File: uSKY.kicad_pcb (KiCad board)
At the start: 2 copper layers, 11.2 x 8.4 mm, 36 parts, among them U1 CC2510, X1 SMD_CRYSTAL_4PIN

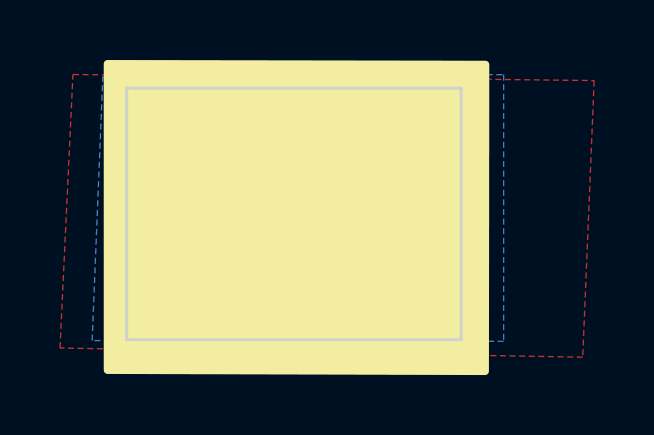
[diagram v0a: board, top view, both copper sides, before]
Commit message: removed silkscreen filled zone
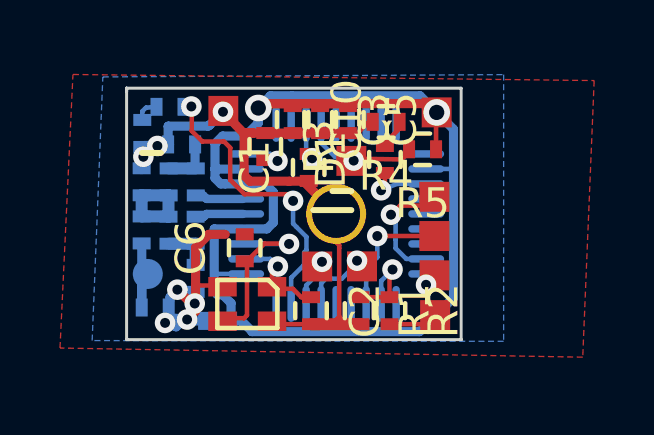
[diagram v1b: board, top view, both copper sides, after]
